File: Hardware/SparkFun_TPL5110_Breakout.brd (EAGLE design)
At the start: 25.4 x 25.4 mm, 61 parts, among them Q1 1.1A/60V/600mΩ, SW1 DIP-06, U1 TPL5110

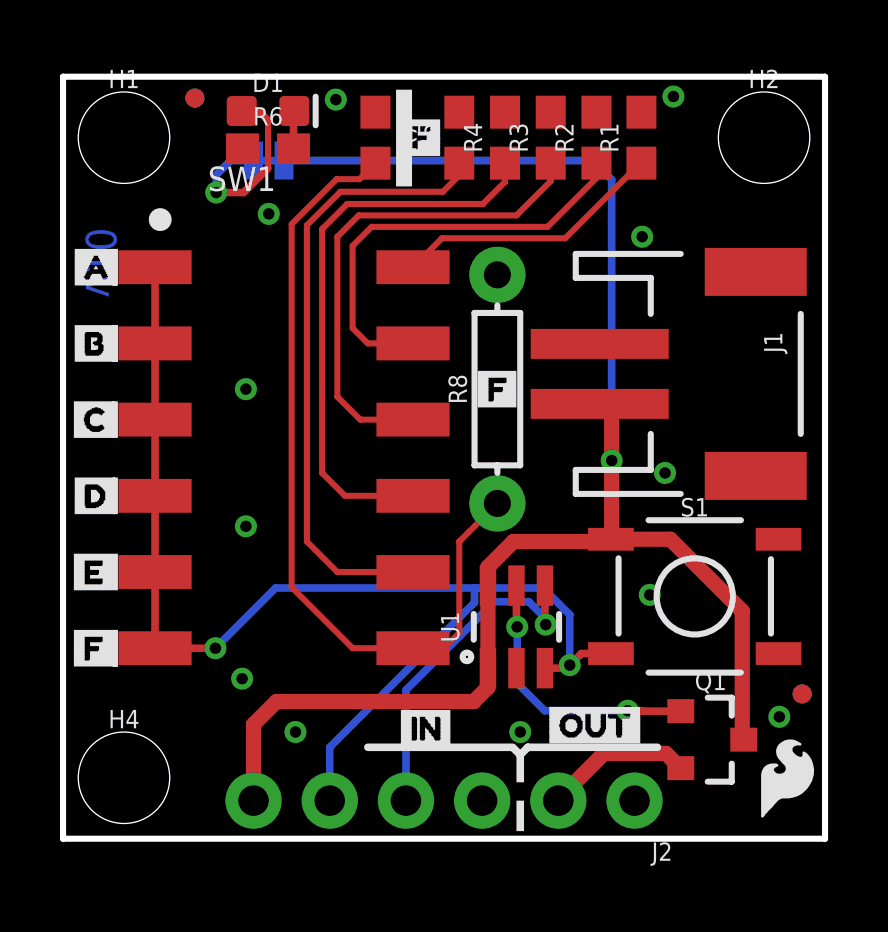
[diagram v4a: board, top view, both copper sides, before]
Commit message: Adds final resistor values: 93.1k, 124k, 169k, Updates python script so that user can calculate combinations with 6th custom resistor
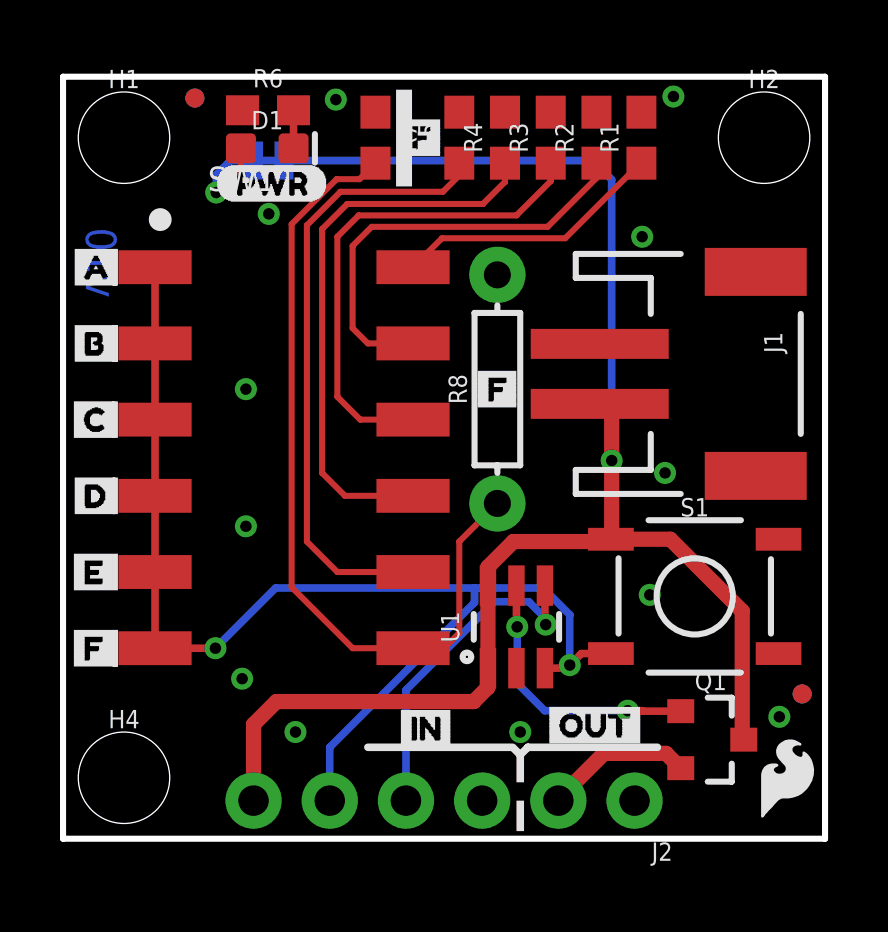
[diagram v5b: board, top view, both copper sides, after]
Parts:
- added U$35: (no value), Labels:PWR-()-03
- R3: value 5.6k -> 93.1k
- R4: value 5.6k -> 124k
- R5: value 5.6k -> 169K
- moved R6 1.27 mm to (6.83, 24.3)
- moved D1 1.24 mm to (6.81, 23.0)
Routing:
- net N$11: track 6.69 -> 3.84 mm
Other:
- board text added: "Units in Inches"
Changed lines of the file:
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@@
 <wire x1="15.24" y1="2.794" x2="15.494" y2="3.048" width="0.254" layer="21"/>
 <wire x1="15.494" y1="3.048" x2="19.812" y2="3.048" width="0.254" layer="21"/>
+<dimension x1="0" y1="25.4" x2="25.4" y2="25.4" x3="12.7" y3="30.226" textsize="1.778" textratio="15" layer="47" dtype="horizontal" unit="inch"/>
+<dimension x1="0" y1="25.4" x2="0" y2="0" x3="-6.35" y3="12.7" textsize="1.778" textratio="15" layer="47" dtype="horizontal" unit="inch"/>
+<dimension x1="2.032" y1="23.368" x2="2.032" y2="25.4" x3="-2.032" y3="24.384" textsize="1.778" textratio="15" layer="47" dtype="horizontal" unit="inch"/>
+<dimension x1="23.368" y1="23.368" x2="25.4" y2="23.622" x3="24.384" y3="26.67" textsize="1.778" textratio="15" layer="47" dtype="horizontal" unit="inch"/>
+<text x="4.572" y="-4.064" size="1.778" layer="47" font="vector" ratio="15">Units in Inches</text>
 </plain>
 <attributes>
@@
 <attribute name="VALUE" value="22k" x="18.542" y="23.368" size="0.6096" layer="27" font="vector" ratio="20" rot="R90" align="top-center"/>
 </element>
-<element name="R3" library="SparkFun-Resistors" package="0603" value="5.6k" x="16.256" y="23.368" smashed="yes" rot="R90">
-<attribute name="NAME" x="15.494" y="23.368" size="0.6096" layer="25" font="vector" ratio="20" rot="R90" align="bottom-center"/>
-<attribute name="PROD_ID" value="RES-12378" x="16.256" y="23.368" size="1.778" layer="27" font="vector" ratio="15" rot="R90" display="off"/>
-<attribute name="VALUE" x="17.018" y="23.368" size="0.6096" layer="27" font="vector" ratio="20" rot="R90" align="top-center"/>
-</element>
-<element name="R4" library="SparkFun-Resistors" package="0603" value="5.6k" x="14.732" y="23.368" smashed="yes" rot="R90">
+<element name="R4" library="SparkFun-Resistors" package="0603" value="124k" x="14.732" y="23.368" smashed="yes" rot="R90">
 <attribute name="NAME" x="13.97" y="23.368" size="0.6096" layer="25" font="vector" ratio="20" rot="R90" align="bottom-center"/>
-<attribute name="PROD_ID" value="RES-12378" x="14.732" y="23.368" size="1.778" layer="27" font="vector" ratio="15" rot="R90" display="off"/>
-<attribute name="VALUE" x="15.494" y="23.368" size="0.6096" layer="27" font="vector" ratio="20" rot="R90" align="top-center"/>
-</element>
-<element name="R5" library="SparkFun-Resistors" package="0603" value="5.6k" x="13.208" y="23.368" smashed="yes" rot="R90">
+<attribute name="PROD_ID" value="RES-14395" x="14.732" y="23.368" size="1.778" layer="27" font="vector" ratio="15" rot="R90" display="off"/>
+<attribute name="VALUE" value="124k" x="15.494" y="23.368" size="0.6096" layer="27" font="vector" ratio="20" rot="R90" align="top-center"/>
+</element>
+<element name="R5" library="SparkFun-Resistors" package="0603" value="169K" x="13.208" y="23.368" smashed="yes" rot="R90">
 <attribute name="NAME" x="12.446" y="23.368" size="0.6096" layer="25" font="vector" ratio="20" rot="R90" align="bottom-center"/>
-<attribute name="PROD_ID" value="RES-12378" x="13.208" y="23.368" size="1.778" layer="27" font="vector" ratio="15" rot="R90" display="off"/>
-<attribute name="VALUE" x="13.97" y="23.368" size="0.6096" layer="27" font="vector" ratio="20" rot="R90" align="top-center"/>
-</element>
-<element name="R6" library="SparkFun-Resistors" package="0603" value="330" x="6.8326" y="23.0124" smashed="yes">
-<attribute name="NAME" x="6.8326" y="23.7744" size="0.6096" layer="25" font="vector" ratio="20" align="bottom-center"/>
-<attribute name="PROD_ID" value="RES-00818" x="6.8326" y="23.0124" size="1.778" layer="27" font="vector" ratio="15" display="off"/>
-<attribute name="VALUE" x="6.8326" y="22.2504" size="0.6096" layer="27" font="vector" ratio="20" align="top-center"/>
-</element>
-<element name="D1" library="SparkFun-LED" package="LED-0603" value="RED" x="6.8326" y="24.257" smashed="yes">
-<attribute name="NAME" x="6.8326" y="24.892" size="0.6096" layer="25" font="vector" ratio="20" align="bottom-center"/>
-<attribute name="PROD_ID" value="DIO-00819" x="6.8326" y="24.257" size="1.778" layer="27" font="vector" ratio="15" display="off"/>
-<attribute name="VALUE" x="6.8326" y="23.622" size="0.6096" layer="27" font="vector" ratio="20" align="top-center"/>
+<attribute name="PROD_ID" value="RES-14394" x="13.208" y="23.368" size="1.778" layer="27" font="vector" ratio="15" rot="R90" display="off"/>
+<attribute name="VALUE" value="169K" x="13.97" y="23.368" size="0.6096" layer="27" font="vector" ratio="20" rot="R90" align="top-center"/>
+</element>
+<element name="R6" library="SparkFun-Resistors" package="0603" value="330" x="6.8326" y="24.2824" smashed="yes">
+<attribute name="NAME" x="6.8326" y="25.0444" size="0.6096" layer="25" font="vector" ratio="20" align="bottom-center"/>
+<attribute name="PROD_ID" value="RES-00818" x="6.8326" y="24.2824" size="1.778" layer="27" font="vector" ratio="15" display="off"/>
+<attribute name="VALUE" x="6.8326" y="23.5204" size="0.6096" layer="27" font="vector" ratio="20" align="top-center"/>
+</element>
+<element name="D1" library="SparkFun-LED" package="LED-0603" value="RED" x="6.8072" y="23.0124" smashed="yes">
+<attribute name="NAME" x="6.8072" y="23.6474" size="0.6096" layer="25" font="vector" ratio="20" align="bottom-center"/>
+<attribute name="PROD_ID" value="DIO-00819" x="6.8072" y="23.0124" size="1.778" layer="27" font="vector" ratio="15" display="off"/>
+<attribute name="VALUE" x="6.8072" y="22.3774" size="0.6096" layer="27" font="vector" ratio="20" align="top-center"/>
 </element>
 <element name="J1" library="SparkFun-Connectors" package="JST-2-SMD" value="" x="21.59" y="15.494" smashed="yes" rot="R270">
@@
 <element name="U$6" library="Nano Power" package="NANO_POWER0" value="" x="23.876" y="6.096" smashed="yes" rot="MR90"/>
 <element name="U$7" library="Switch" package="SWITCH0" value="" x="21.844" y="8.89" smashed="yes" rot="MR90"/>
+<element name="R3" library="SparkFun-Resistors" package="0603" value="93.1k" x="16.256" y="23.368" smashed="yes" rot="R90">
+<attribute name="NAME" x="15.494" y="23.368" size="0.6096" layer="25" font="vector" ratio="20" rot="R90" align="bottom-center"/>
+<attribute name="PROD_ID" value="RES-14393" x="16.256" y="23.368" size="1.778" layer="27" font="vector" ratio="15" rot="R90" display="off"/>
+<attribute name="VALUE" x="17.018" y="23.368" size="0.6096" layer="27" font="vector" ratio="20" rot="R90" align="top-center"/>
+</element>
+<element name="U$35" library="Labels" package="PWR-()-03" value="" x="5.08" y="21.844" smashed="yes"/>
 </elements>
 <signals>
@@
 <contactref element="R6" pad="1"/>
 <contactref element="R2" pad="2"/>
-<contactref element="R3" pad="2"/>
 <contactref element="R4" pad="2"/>
 <contactref element="R5" pad="2"/>
@@
 <via x="20.066" y="12.192" extent="1-16" drill="0.381"/>
 <via x="5.969" y="5.334" extent="1-16" drill="0.381"/>
+<contactref element="R3" pad="2"/>
 </signal>
 <signal name="VDD">
@@
 <contactref element="R6" pad="2"/>
 <contactref element="D1" pad="C"/>
-<wire x1="7.7096" y1="24.257" x2="7.6826" y2="24.23" width="0.254" layer="1"/>
-<wire x1="7.6826" y1="24.23" x2="7.6826" y2="23.0124" width="0.254" layer="1"/>
+<wire x1="7.6826" y1="24.2824" x2="7.6826" y2="23.014" width="0.254" layer="1"/>
+<wire x1="7.6842" y1="23.0124" x2="7.6826" y2="23.014" width="0.254" layer="1"/>
 </signal>
 <signal name="N$5">
@@
 </signal>
 <signal name="N$6">
-<contactref element="R3" pad="1"/>
 <contactref element="SW1" pad="10"/>
 <wire x1="11.666" y1="13.97" x2="9.906" y2="13.97" width="0.2032" layer="1"/>
@@
 <wire x1="9.144" y1="20.066" x2="9.8552" y2="20.7772" width="0.2032" layer="1"/>
 <wire x1="9.8552" y1="20.7772" x2="15.113" y2="20.7772" width="0.2032" layer="1"/>
-<wire x1="16.256" y1="22.518" x2="16.256" y2="21.9202" width="0.2032" layer="1"/>
-<wire x1="16.256" y1="21.9202" x2="15.113" y2="20.7772" width="0.2032" layer="1"/>
+<contactref element="R3" pad="1"/>
+<wire x1="15.113" y1="20.7772" x2="16.256" y2="21.9202" width="0.2032" layer="1"/>
+<wire x1="16.256" y1="21.9202" x2="16.256" y2="22.518" width="0.2032" layer="1"/>
 </signal>
 <signal name="N$9">
@@
 <contactref element="JP2" pad="1"/>
 <via x="5.1054" y="21.5392" extent="1-16" drill="0.381"/>
-<wire x1="5.9556" y1="24.257" x2="6.5144" y2="24.257" width="0.254" layer="1"/>
-<wire x1="6.8326" y1="23.9388" x2="6.5144" y2="24.257" width="0.254" layer="1"/>
-<wire x1="6.8326" y1="23.9388" x2="6.8326" y2="22.352" width="0.2032" layer="1"/>
-<wire x1="5.1054" y1="21.5392" x2="6.0198" y2="21.5392" width="0.254" layer="1"/>
-<wire x1="6.8326" y1="22.352" x2="6.0198" y2="21.5392" width="0.254" layer="1"/>
 <wire x1="5.1054" y1="21.5392" x2="5.1054" y2="22.1234" width="0.254" layer="16"/>
 <wire x1="5.1054" y1="22.1234" x2="5.588" y2="22.606" width="0.254" layer="16"/>
 <wire x1="5.588" y1="22.606" x2="6.35" y2="22.606" width="0.254" layer="16"/>
+<wire x1="5.9302" y1="23.0124" x2="5.9302" y2="22.364" width="0.2032" layer="1"/>
+<wire x1="5.9302" y1="22.364" x2="5.1054" y2="21.5392" width="0.2032" layer="1"/>
 </signal>
 <signal name="DONE">
